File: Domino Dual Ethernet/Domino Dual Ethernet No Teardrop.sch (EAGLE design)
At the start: 38 parts, among them J1 HBJ-2H101NLF, J2 MH18-1, J3 MH18-1

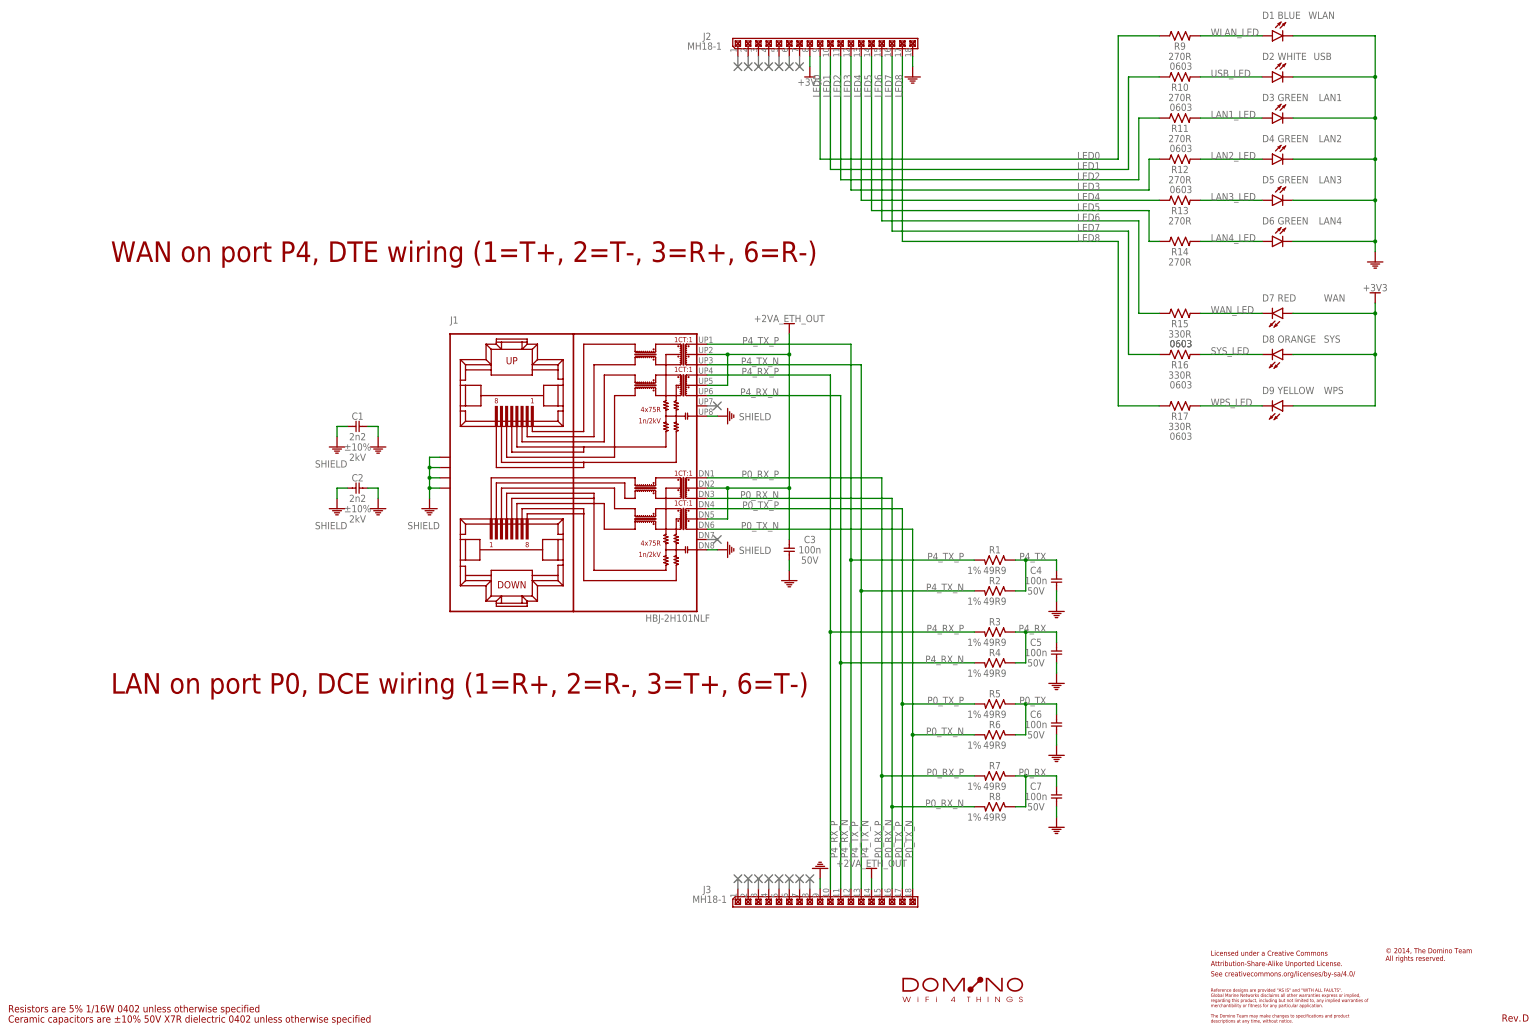
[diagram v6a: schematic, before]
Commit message: Added UART header to both Ethernet tiles
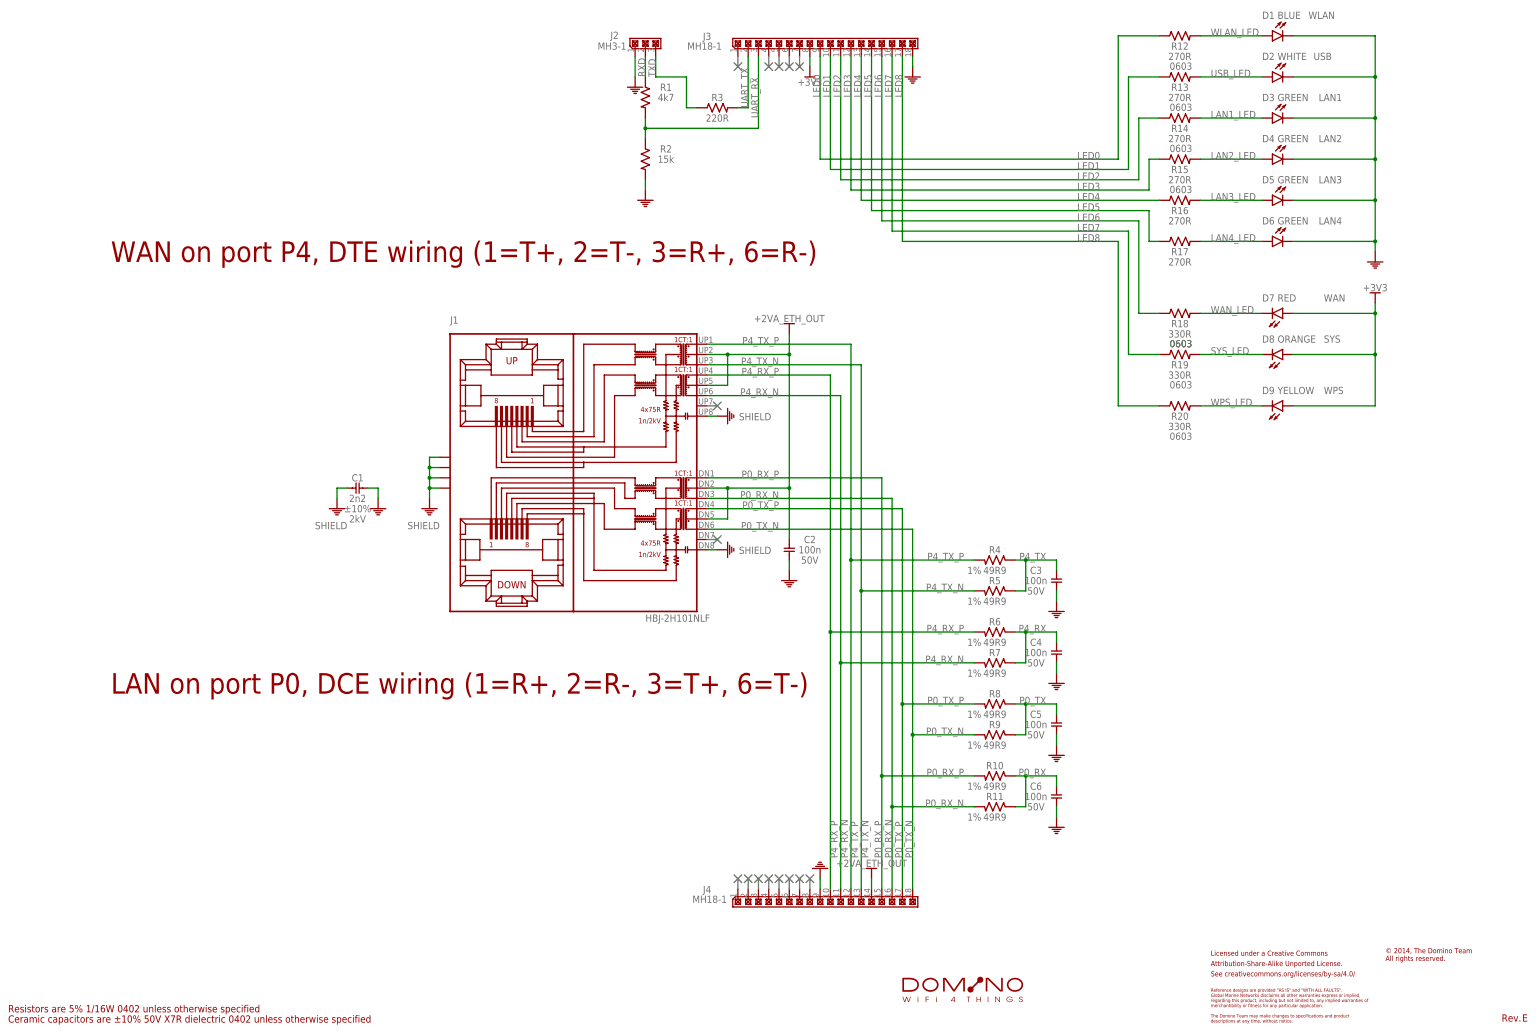
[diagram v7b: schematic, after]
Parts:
- removed C7: 100n, Domino:CAP_0402
- added J4: MH18-1, Domino:MH18-1
- added R18, R19, R20: 330R, Domino:RES_0603
- C2: value 2n2 -> 100n; device Domino:CAP_1206 -> Domino:CAP_0402; PARTNO C1210_2n2_X7R_10%_CER_2kV -> C0402_100n_X7R_10%_CER_50V; VOLT 2kV -> 50V
- J2: value MH18-1 -> MH3-1; device Domino:MH18-1 -> Domino:MH3-1; PARTNO MH18-1-0.1 -> MH3-1-0.1
- R1: value 49R9 -> 4k7; PARTNO R0402_49R9_1%_62.5mW -> R0402_4k7_5%_62.5mW; TOL 1% -> 5%
- R10, R11, R9: value 270R -> 49R9; device Domino:RES_0603 -> Domino:RES_0402; PARTNO R0603_270R_5%_125mW -> R0402_49R9_1%_62.5mW; RATE 125mW -> 62.5mW; TOL 5% -> 1%
- R15, R16, R17: value 330R -> 270R; PARTNO R0603_330R_5%_125mW -> R0603_270R_5%_125mW
- R2: value 49R9 -> 15k; PARTNO R0402_49R9_1%_62.5mW -> R0402_15k_5%_62.5mW; TOL 1% -> 5%
- R3: value 49R9 -> 220R; PARTNO R0402_49R9_1%_62.5mW -> R0402_220R_5%_62.5mW; TOL 1% -> 5%
- renumbered U$10 to L1
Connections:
- new net RXD: J2.2, R1.1
- new net TXD: J2.3, R3.1
- new net UART_RX: J3.3, R1.2, R2.1
- new net UART_TX: J3.2, R3.2
- net +2VA_ETH_OUT: now also C2.2, J4.14; no longer C3.2, J3.14
- net +3V3: now also J3.8; no longer J2.8
- net GND: now also J2.1, J3.18, J4.9, R2.2; no longer C7.1, J2.18, J3.9
- net LAN1_LED: now also R14.2; no longer R11.2
- net LAN2_LED: now also R15.2; no longer R12.2
- net LAN3_LED: now also R16.2; no longer R13.2
- net LAN4_LED: now also R17.2; no longer R14.2
- net LED0: now also J3.9, R12.1; no longer J2.9, R9.1
- net LED1: now also J3.10, R13.1; no longer J2.10, R10.1
- net LED2: now also J3.11, R14.1; no longer J2.11, R11.1
- net LED3: now also J3.12, R15.1; no longer J2.12, R12.1
- net LED4: now also J3.13, R16.1; no longer J2.13, R13.1
- net LED5: now also J3.14, R17.1; no longer J2.14, R14.1
- net LED6: now also J3.15, R18.1; no longer J2.15, R15.1
- net LED7: now also J3.16, R19.1; no longer J2.16, R16.1
- net LED8: now also J3.17, R20.1; no longer J2.17, R17.1
- net P0_RX: now also C6.2, R10.1, R11.1; no longer C7.2, R7.1, R8.1
- net P0_RX_N: now also J4.16, R11.2; no longer J3.16, R8.2
- net P0_RX_P: now also J4.15, R10.2; no longer J3.15, R7.2
- net P0_TX: now also C5.2, R8.1, R9.1; no longer C6.2, R5.1, R6.1
- net P0_TX_N: now also J4.18, R9.2; no longer J3.18, R6.2
- net P0_TX_P: now also J4.17, R8.2; no longer J3.17, R5.2
- net P4_RX: now also C4.2, R6.1, R7.1; no longer C5.2, R3.1, R4.1
- net P4_RX_N: now also J4.11, R7.2; no longer J3.11, R4.2
- net P4_RX_P: now also J4.10, R6.2; no longer J3.10, R3.2
- net P4_TX: now also C3.2, R4.1, R5.1; no longer C4.2, R1.1, R2.1
- net P4_TX_N: now also J4.13, R5.2; no longer J3.13, R2.2
- net P4_TX_P: now also J4.12, R4.2; no longer J3.12, R1.2
- net SHIELD: no longer C2.2
- net SYS_LED: now also R19.2; no longer R16.2
- net USB_LED: now also R13.2; no longer R10.2
- net WAN_LED: now also R18.2; no longer R15.2
- net WLAN_LED: now also R12.2; no longer R9.2
- net WPS_LED: now also R20.2; no longer R17.2
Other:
- moved on the sheet: C1, C2, C3, C4, C5, C6, J3, R1, R10, R11, R12, R13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
